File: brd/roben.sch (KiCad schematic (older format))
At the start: 72 parts, among them J1 POWER IN, J10 1+, J11 1-, J12 2-, J13 2+, J2 +V, J3 GND, J4 +V, J5 GND, J6 A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

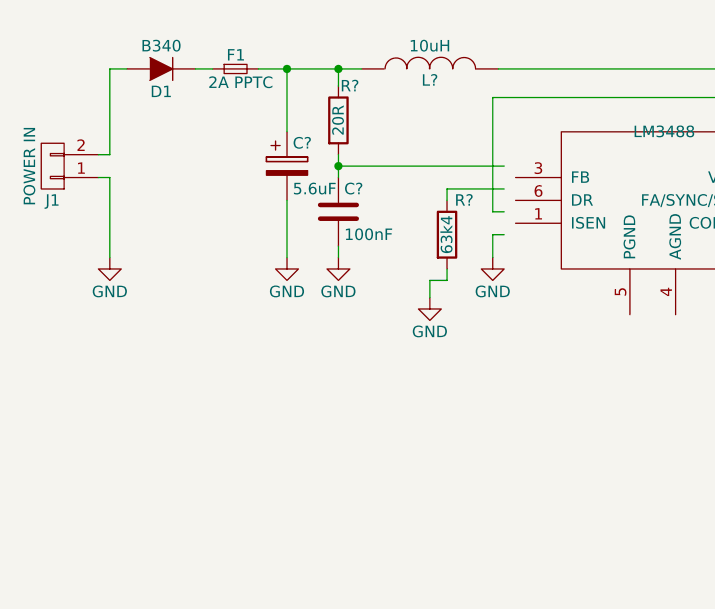
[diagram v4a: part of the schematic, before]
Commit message: new: añadido interruptor de encendido, segun #6
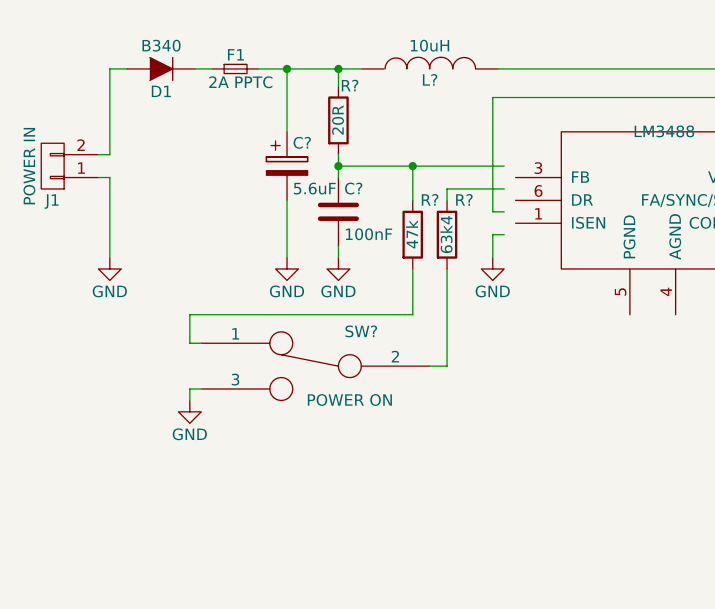
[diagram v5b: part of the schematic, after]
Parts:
- added R?: 47k, symbol R
- added SW?: POWER ON, symbol SWITCH_INV
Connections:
- wire segments 237 -> 243
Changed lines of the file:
@@
-$Comp
-L GND #PWR?
-U 1 1 569D1AF1
-P 2375 1925
-F 0 "#PWR?" H 2375 1675 50  0001 C CNN
-F 1 "GND" H 2375 1775 50  0000 C CNN
-F 2 "" H 2375 1925 50  0000 C CNN
-F 3 "" H 2375 1925 50  0000 C CNN
-	1    2375 1925
-	1    0    0    -1
-$EndComp
 $Comp
 L GND #PWR?
@@
 Wire Wire Line
 	2450 1500 2450 1450
-Wire Wire Line
-	2375 1850 2450 1850
-Wire Wire Line
-	2450 1850 2450 1800
-Wire Wire Line
-	2375 1925 2375 1850
 Wire Wire Line
 	1975 1350 2700 1350
@@
 	8600 4500 8600 4675
 Connection ~ 8850 4675
+$Comp
+L R R?
+U 1 1 569EAA1D
+P 2300 1650
+F 0 "R?" H 2375 1800 50  0000 C CNN
+F 1 "47k" V 2300 1650 50  0000 C CNN
+F 2 "" V 2230 1650 50  0000 C CNN
+F 3 "" H 2300 1650 50  0000 C CNN
+	1    2300 1650
+	1    0    0    -1
+$EndComp
+Wire Wire Line
+	2300 1500 2300 1350
+Connection ~ 2300 1350
+$Comp
+L SWITCH_INV SW?
+U 1 1 569EAD89
+P 1875 2225
+F 0 "SW?" H 1675 2375 50  0000 C CNN
+F 1 "POWER ON" H 1725 2075 50  0000 C CNN
+F 2 "" H 1875 2225 50  0000 C CNN
+F 3 "" H 1875 2225 50  0000 C CNN
+	1    1875 2225
+	-1   0    0    -1
+$EndComp
+$Comp
+L GND #PWR?
+U 1 1 569EB15F
+P 1325 2375
+F 0 "#PWR?" H 1325 2125 50  0001 C CNN
+F 1 "GND" H 1325 2225 50  0000 C CNN
+F 2 "" H 1325 2375 50  0000 C CNN
+F 3 "" H 1325 2375 50  0000 C CNN
+	1    1325 2375
+	1    0    0    -1
+$EndComp
+Wire Wire Line
+	2450 1800 2450 2225
+Wire Wire Line
+	2450 2225 2375 2225
+Wire Wire Line
+	2300 1800 2300 2000
+Wire Wire Line
+	2300 2000 1325 2000
+Wire Wire Line
+	1325 2000 1325 2125
+Wire Wire Line
+	1325 2125 1375 2125
+Wire Wire Line
+	1325 2375 1325 2325
+Wire Wire Line
+	1325 2325 1375 2325
 $EndSCHEMATC

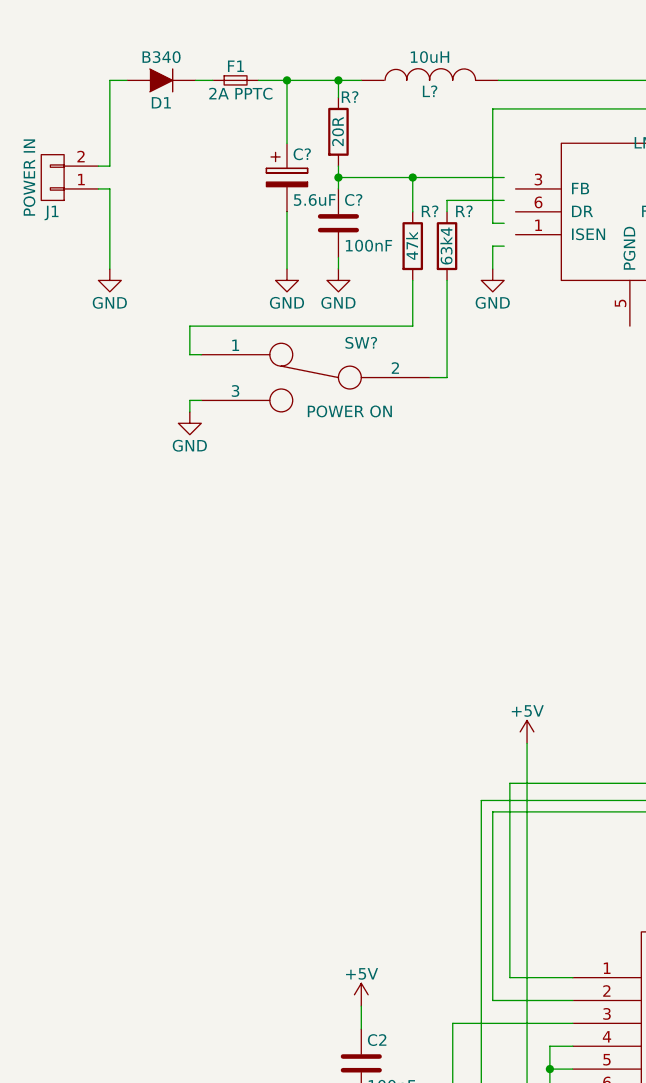
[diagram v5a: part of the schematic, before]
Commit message: new: añadido indicador de bateria baja, segun #7
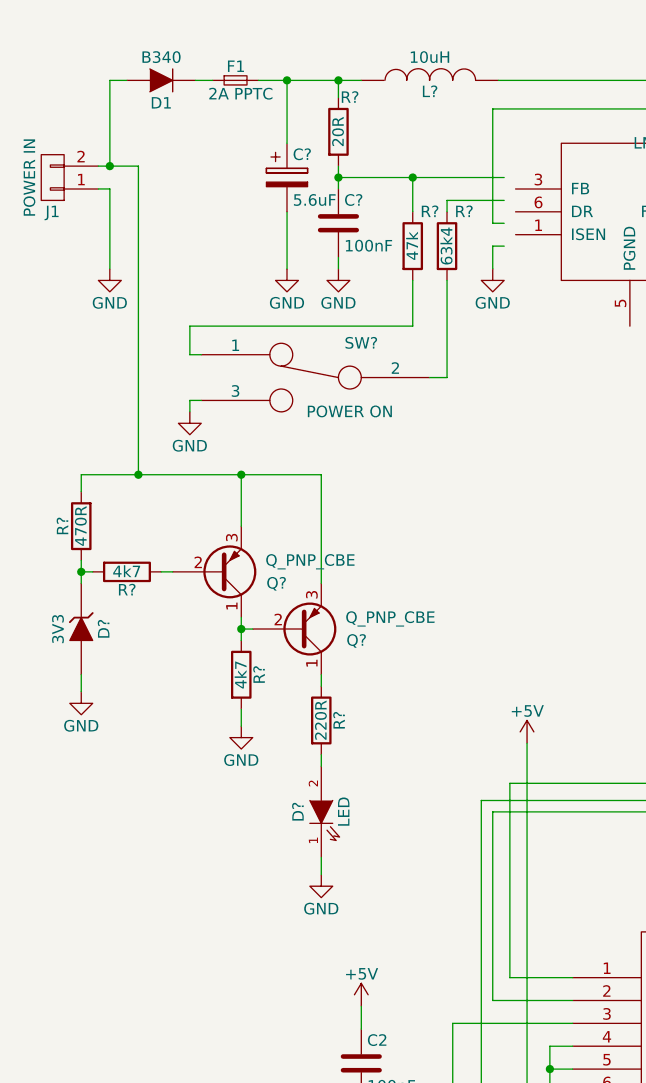
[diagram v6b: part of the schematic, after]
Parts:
- added D?: LED, LEDs:LED-0805, symbol LED
- added D?: 3V3, symbol ZENER
- added Q? (x2): Q_PNP_CBE, symbol Q_PNP_CBE
- added R?: 470R, symbol R
- added R? (x2): 4k7, symbol R
- added R?: 220R, symbol R
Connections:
- wire segments 243 -> 258
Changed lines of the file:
@@
 $EndComp
 Wire Wire Line
-	925  1300 975  1300
+	925  1300 1100 1300
 Wire Wire Line
 	975  1300 975  925
@@
 Wire Wire Line
 	1325 2325 1375 2325
+$Comp
+L Q_PNP_CBE Q?
+U 1 1 569ECFB4
+P 1450 3075
+F 0 "Q?" H 1750 3125 50  0000 R CNN
+F 1 "Q_PNP_CBE" H 2050 3025 50  0000 R CNN
+F 2 "" H 1650 3175 50  0000 C CNN
+F 3 "" H 1450 3075 50  0000 C CNN
+	1    1450 3075
+	1    0    0    1
+$EndComp
+$Comp
+L Q_PNP_CBE Q?
+U 1 1 569ED06D
+P 1800 3325
+F 0 "Q?" H 2100 3375 50  0000 R CNN
+F 1 "Q_PNP_CBE" H 2400 3275 50  0000 R CNN
+F 2 "" H 2000 3425 50  0000 C CNN
+F 3 "" H 1800 3325 50  0000 C CNN
+	1    1800 3325
+	1    0    0    1
+$EndComp
+$Comp
+L R R?
+U 1 1 569ED278
+P 850 2875
+F 0 "R?" V 930 2875 50  0000 C CNN
+F 1 "470R" V 850 2875 50  0000 C CNN
+F 2 "" V 780 2875 50  0000 C CNN
+F 3 "" H 850 2875 50  0000 C CNN
+	1    850  2875
+	-1   0    0    1
+$EndComp
+$Comp
+L R R?
+U 1 1 569ED3F9
+P 1050 3075
+F 0 "R?" V 1130 3075 50  0000 C CNN
+F 1 "4k7" V 1050 3075 50  0000 C CNN
+F 2 "" V 980 3075 50  0000 C CNN
+F 3 "" H 1050 3075 50  0000 C CNN
+	1    1050 3075
+	0    1    1    0
+$EndComp
+$Comp
+L R R?
+U 1 1 569ED4B6
+P 1900 3725
+F 0 "R?" V 1980 3725 50  0000 C CNN
+F 1 "220R" V 1900 3725 50  0000 C CNN
+F 2 "" V 1830 3725 50  0000 C CNN
+F 3 "" H 1900 3725 50  0000 C CNN
+	1    1900 3725
+	1    0    0    -1
+$EndComp
+$Comp
+L R R?
+U 1 1 569ED58B
+P 1550 3525
+F 0 "R?" V 1630 3525 50  0000 C CNN
+F 1 "4k7" V 1550 3525 50  0000 C CNN
+F 2 "" V 1480 3525 50  0000 C CNN
+F 3 "" H 1550 3525 50  0000 C CNN
+	1    1550 3525
+	1    0    0    -1
+$EndComp
+$Comp
+L LED D?
+U 1 1 569ED731
+P 1900 4125
+F 0 "D?" H 1900 4225 50  0000 C CNN
+F 1 "LED" H 1900 4025 50  0000 C CNN
+F 2 "LEDs:LED-0805" H 1900 4125 60  0001 C CNN
+F 3 "" H 1900 4125 60  0000 C CNN
+F 4 "720-LOR976-PS-1" H 1900 4125 60  0001 C CNN "Vendor"
+	1    1900 4125
+	0    -1   -1   0
+$EndComp
+$Comp
+L ZENER D?
+U 1 1 569ED902
+P 850 3325
+F 0 "D?" H 850 3425 50  0000 C CNN
+F 1 "3V3" H 850 3225 50  0000 C CNN
+F 2 "" H 850 3325 50  0000 C CNN
+F 3 "" H 850 3325 50  0000 C CNN
+	1    850  3325
+	0    1    1    0
+$EndComp
+Wire Wire Line
+	850  3025 850  3125
+Wire Wire Line
+	900  3075 850  3075
+Connection ~ 850  3075
+Wire Wire Line
+	1200 3075 1250 3075
+Wire Wire Line
+	1550 3275 1550 3375
+Wire Wire Line
+	1600 3325 1550 3325
+Connection ~ 1550 3325
+Wire Wire Line
+	1900 3525 1900 3575
+Wire Wire Line
+	1900 3875 1900 3925
+$Comp
+L GND #PWR?
+U 1 1 569F0749
+P 850 3600
+F 0 "#PWR?" H 850 3350 50  0001 C CNN
+F 1 "GND" H 850 3450 50  0000 C CNN
+F 2 "" H 850 3600 50  0000 C CNN
+F 3 "" H 850 3600 50  0000 C CNN
+	1    850  3600
+	1    0    0    -1
+$EndComp
+$Comp
+L GND #PWR?
+U 1 1 569F0801
+P 1550 3750
+F 0 "#PWR?" H 1550 3500 50  0001 C CNN
+F 1 "GND" H 1550 3600 50  0000 C CNN
+F 2 "" H 1550 3750 50  0000 C CNN
+F 3 "" H 1550 3750 50  0000 C CNN
+	1    1550 3750
+	1    0    0    -1
+$EndComp
+$Comp
+L GND #PWR?
+U 1 1 569F095D
+P 1900 4400
+F 0 "#PWR?" H 1900 4150 50  0001 C CNN
+F 1 "GND" H 1900 4250 50  0000 C CNN
+F 2 "" H 1900 4400 50  0000 C CNN
+F 3 "" H 1900 4400 50  0000 C CNN
+	1    1900 4400
+	1    0    0    -1
+$EndComp
+Wire Wire Line
+	1900 4400 1900 4325
+Wire Wire Line
+	1550 3750 1550 3675
+Wire Wire Line
+	850  3525 850  3600
+Wire Wire Line
+	1900 3125 1900 2650
+Wire Wire Line
+	1900 2650 850  2650
+Wire Wire Line
+	850  2650 850  2725
+Wire Wire Line
+	1550 2875 1550 2650
+Connection ~ 1550 2650
+Wire Wire Line
+	1100 1300 1100 2650
+Connection ~ 1100 2650
+Connection ~ 975  1300
 $EndSCHEMATC

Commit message: chg: optimizado esquemático y circuito
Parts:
- removed D4, D5, D6: 5V1, Diodes_SMD:SOD-123, symbol ZENER
- removed D? (x3): LED, LEDs:LED-0805, symbol LED
- removed D?: 3V3, symbol ZENER
- removed J7: B, Wire_Pads:SolderWirePad_single_2-5mmDrill, symbol CONN_01X01
- removed J8: C, Wire_Pads:SolderWirePad_single_2-5mmDrill, symbol CONN_01X01
- removed J9: D, Wire_Pads:SolderWirePad_single_2-5mmDrill, symbol CONN_01X01
- removed Q?: DMN6068LK3-13, symbol Q_NMOS_GDS
- removed Q?: Q_PNP_CBE, symbol Q_PNP_CBE
- removed R6, R7, R9, R? (x3): 220R, Resistors_SMD:R_0805_HandSoldering, symbol R
- removed R?: 470R, symbol R
- removed R?: 4k7, symbol R
- removed U? (x3): LM2902N, symbol LM2902N
- added C?: 470uF, symbol CP
- added D?: D, symbol D
- added D? (x3): 5V1, Diodes_SMD:SOD-123, symbol ZENER
- added D? (x3): LED, LEDs:LED-0805, symbol LED
- added J?: B, Wire_Pads:SolderWirePad_single_2-5mmDrill, symbol CONN_01X01
- added J?: C, Wire_Pads:SolderWirePad_single_2-5mmDrill, symbol CONN_01X01
- added J?: D, Wire_Pads:SolderWirePad_single_2-5mmDrill, symbol CONN_01X01
- added Q?: BUK7Y98, LFPAK56, symbol IRF8721PBF-1
- added R? (x6): 220R, Resistors_SMD:R_0805_HandSoldering, symbol R
- added U? (x3): LM2902N, symbol LM2902N
- C?: Vendor (none) -> C0805C104K5RACTU
- C?: value 2.4nF -> 1.6nF; Vendor (none) -> GRM2165C1H162JA01D
- C?: value 100nF -> 390nF; Vendor (none) -> VJ0805Y394KXJTW1BC
- C?: Vendor (none) -> UMK316AB7475KL-T
- C?: value 1.2nF -> 2.4nF; Vendor (none) -> GRM2165C1H242JA01D
- C?: value 5.6uF -> 10uF; Vendor (none) -> VE-100M1HTR-0505
- C?: value 330uF -> 470uF; Vendor (none) -> UWT1A471MNL1GS
- D1: Vendor 621-B340-F -> B340-13-F
- D8: value LED -> BLUE; Vendor 720-LOR976-PS-1 -> LB Q39G-L2N2-35-1
- D?: value B540 -> SD2114S040S8R0; Vendor B540C-13-F -> SD2114S040S8R0
- D?: value LED -> ORANGE; Vendor 720-LOR976-PS-1 -> LO R976-PS-1
- F1: value 2A PPTC -> 1.5A PPTC; Vendor 530-0ZCF0200FF2C -> 0ZCF0150FF2C
- J1: Vendor 651-1985946 -> 1776493-2 / RAPC722X
- L?: value 33uH -> 68uH; Vendor (none) -> SDR1307-680KL
- L?: value 10uH -> 22uH; Vendor (none) -> SRR1210-220M
- Q?: value Q_PNP_CBE -> BC856; Vendor (none) -> BC856A-T
- R10: Vendor 71-CRCW0805-220-E3 -> ERJ-6GEYJ221V
- R?: Vendor (none) -> ERJ-6ENF20R0V
- R?: value 1k58 -> 1k96; Vendor (none) -> ERJ-6ENF1961V
- R?: Vendor (none) -> ERJ-6ENF2942V
- R?: Vendor (none) -> ERJ-6ENF1002V
- R?: value 63k4 -> 154k; Vendor (none) -> ERJ-6ENF1543V
- R?: Vendor (none) -> KRL1632E-M-R018-F-T5
- R?: Vendor (none) -> ERJ-6ENF1000V
- R?: value 47k -> 10k; Vendor (none) -> ERJ-6ENF1002V
- R?: Vendor (none) -> ERJ-6GEYJ221V
- R?: value 4k7 -> 10k; Vendor (none) -> ERJ-6ENF1002V
- SW?: Vendor (none) -> JS202011SCQN
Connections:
- net +5V: now also C?.1, D?.2 (A)
- net GND: now also U?.4 (AGND), U?.5 (PGND), C?.2, D?.1 (K), D?.1 (K), D?.1 (K), D?.2 (A), D?.2 (A), D?.2 (A), U?.11 (V-); no longer R?.2
- net D7: now reaches U2.1 (1,2EN), U3.10 (D7)
- net D9: now reaches U2.10 (3A), U3.12 (D9*)
- net D10: now reaches U2.15 (4A), U3.13 (D10*)
- net D5: now reaches U2.2 (1A), U3.8 (D5*)
- net D6: now reaches U2.7 (2A), U3.9 (D6*)
- net D8: now reaches U2.9 (3,4EN), U3.11 (D8)
- net at D1.2 (A), J1.2 (P2): no longer Q?.3 (E)
- net at D1.1 (K), F1.1: now also R?.2
- net A2: now reaches D3.1 (K), R8.2, U3.21 (A2), U3.5 (D2), U?.3 (+)
- net A5: now reaches U3.16 (D13), U3.24 (A5)
- net A5: now also D?.1 (K), R?.2, U?.10 (+)
- net A3: now reaches U3.22 (A3), U3.6 (D3*)
- net A3: now also D?.1 (K), R?.2, U?.5 (+)
- net A4: now reaches U3.14 (D11*), U3.23 (A4)
- net A4: now also D?.1 (K), R?.2, U?.12 (+)
- net at U?.1 (ISEN): now also C?.1, R?.2
- net at U?.2 (COMP): now also C?.1, R?.1
- net at U?.3 (FB): now also R?.1, R?.2
- net at U?.6 (DR): now also Q?.4 (G)
- net at U?.7 (FA/SYNC/SD): now also R?.1
- net at U?.8 (VIN): now also C?.1, R?.1, R?.2
- net at C?.2, L?.2: now also Q?.5, Q?.6, Q?.7, Q?.8 (D)
- net at R?.2, SW?.2: now also R?.2
- net at R?.1, R?.1: now also Q?.1 (S), Q?.2, Q?.3
- net at SW?.1: no longer R?.2
- new net: D?.1 (K), Q?.3 (E)
- new net: J?.1 (P1), R?.1 (x3)
- new net: R?.2, U?.6 (-), U?.7
- new net: D?.2 (A), R?.1 (x3)
- new net: R?.2, U?.8, U?.9 (-)
- new net: R?.2, U?.13 (-), U?.14
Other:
- note added: "Warn @ 4V"
- moved on the sheet: C2, C?, D1, D3, D7, D8, D?, F1, J1, J10, J11, J12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

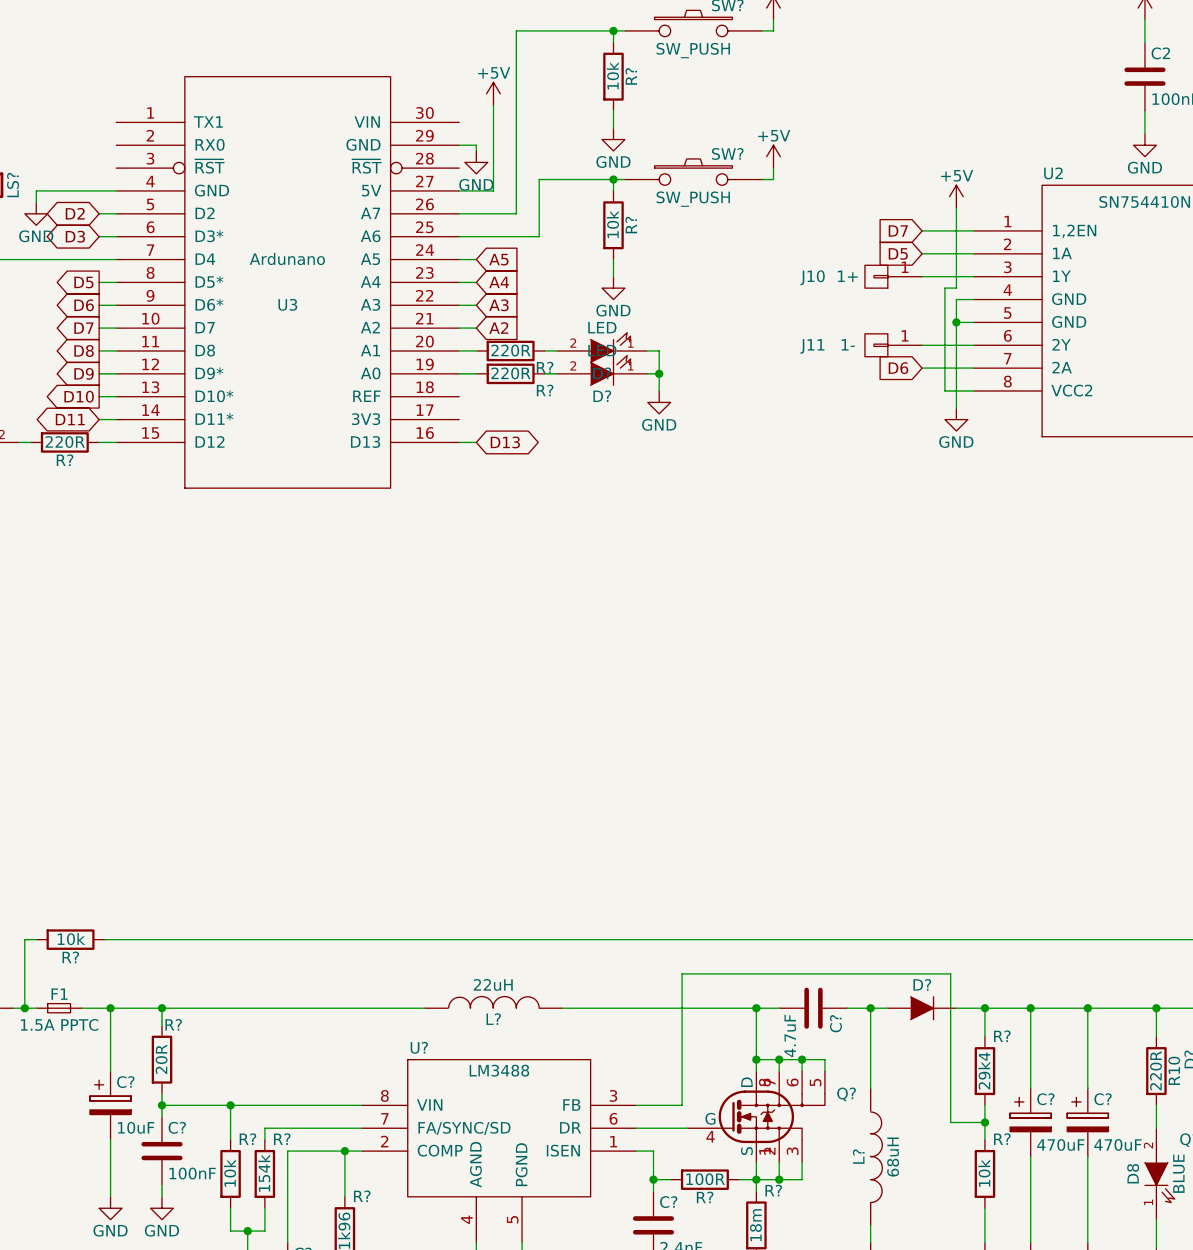
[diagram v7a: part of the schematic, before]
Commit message: chg: añadido seleccion de tension para motores
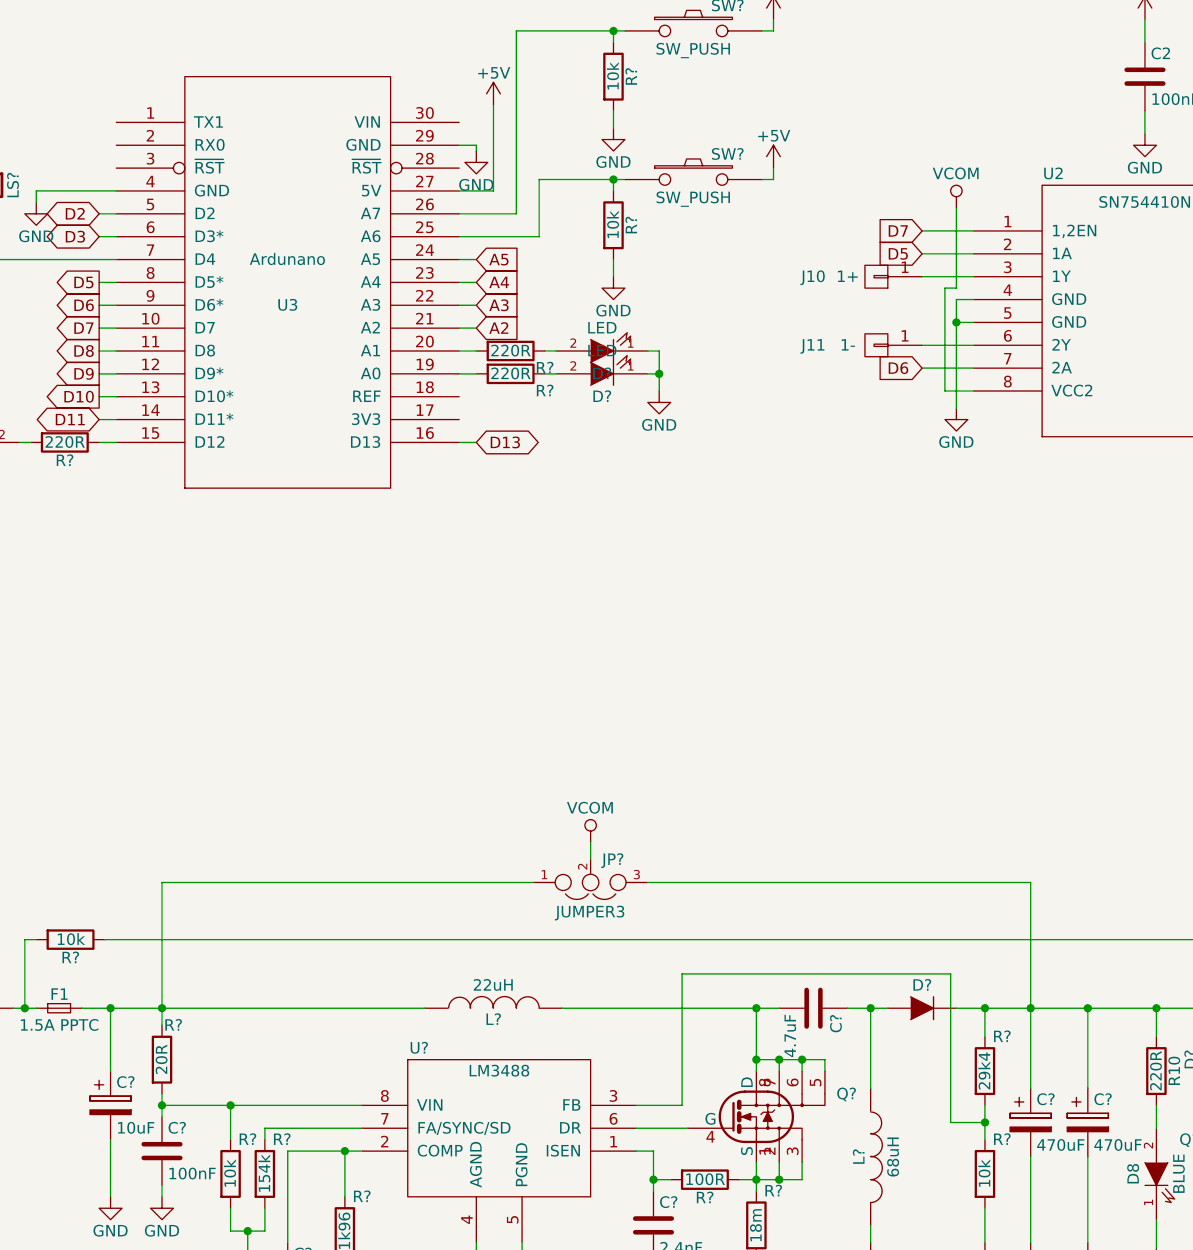
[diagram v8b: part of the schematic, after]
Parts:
- added JP?: JUMPER3, symbol JUMPER3
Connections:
- net +5V: now also JP?.3; no longer U2.8 (VCC2)
- net at C?.1, F1.2, L?.1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: now also JP?.1
- new net VCOM: JP?.2, U2.8 (VCC2)
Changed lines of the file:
@@
 	5300 2825 5525 2825
 Wire Wire Line
-	5775 6075 5775 5725
-Wire Wire Line
-	1975 5800 1975 5725
+	5775 5175 5775 6075
+Wire Wire Line
+	1975 5175 1975 5800
 $Comp
 L +5V #PWR?
@@
 $Comp
 L +5V #PWR?
-U 1 1 56A4F2EB
-P 5450 2225
-F 0 "#PWR?" H 5450 2075 50  0001 C CNN
-F 1 "+5V" H 5450 2365 50  0000 C CNN
-F 2 "" H 5450 2225 60  0000 C CNN
-F 3 "" H 5450 2225 60  0000 C CNN
-	1    5450 2225
-	1    0    0    -1
-$EndComp
-$Comp
-L +5V #PWR?
 U 1 1 56A4F576
 P 7100 2225
@@
 Wire Wire Line
 	10025 4325 10025 4650
+$Comp
+L VCOM #PWR?
+U 1 1 56A67311
+P 3850 5000
+F 0 "#PWR?" H 3850 4850 50  0001 C CNN
+F 1 "VCOM" H 3850 5150 50  0000 C CNN
+F 2 "" H 3850 5000 50  0000 C CNN
+F 3 "" H 3850 5000 50  0000 C CNN
+	1    3850 5000
+	1    0    0    -1
+$EndComp
+$Comp
+L JUMPER3 JP?
+U 1 1 56A673C5
+P 3850 5175
+F 0 "JP?" H 3900 5075 50  0000 L CNN
+F 1 "JUMPER3" H 3850 5275 50  0000 C BNN
+F 2 "" H 3850 5175 50  0000 C CNN
+F 3 "" H 3850 5175 50  0000 C CNN
+	1    3850 5175
+	1    0    0    1
+$EndComp
+$Comp
+L VCOM #PWR?
+U 1 1 56A67EBA
+P 5450 2225
+F 0 "#PWR?" H 5450 2075 50  0001 C CNN
+F 1 "VCOM" H 5450 2375 50  0000 C CNN
+F 2 "" H 5450 2225 50  0000 C CNN
+F 3 "" H 5450 2225 50  0000 C CNN
+	1    5450 2225
+	1    0    0    -1
+$EndComp
+Wire Wire Line
+	3600 5175 1975 5175
+Wire Wire Line
+	4100 5175 5775 5175
+Wire Wire Line
+	3850 5000 3850 5075
 $EndSCHEMATC
